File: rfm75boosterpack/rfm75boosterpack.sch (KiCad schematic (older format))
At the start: 4 parts, among them J1 Ti_Booster_J1, U1 RFM75

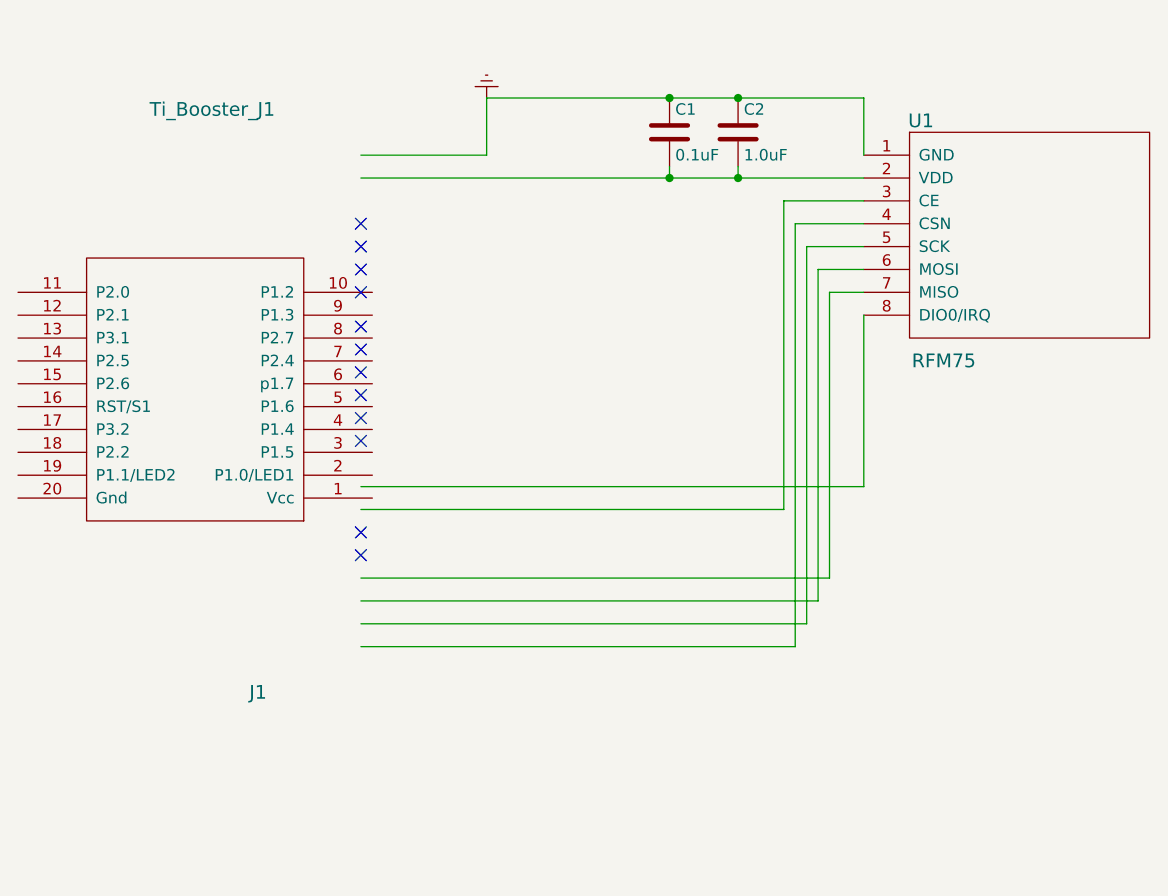
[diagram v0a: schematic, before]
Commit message: Correct boosterpack component, replace, and reroute. Also regen gerbers.
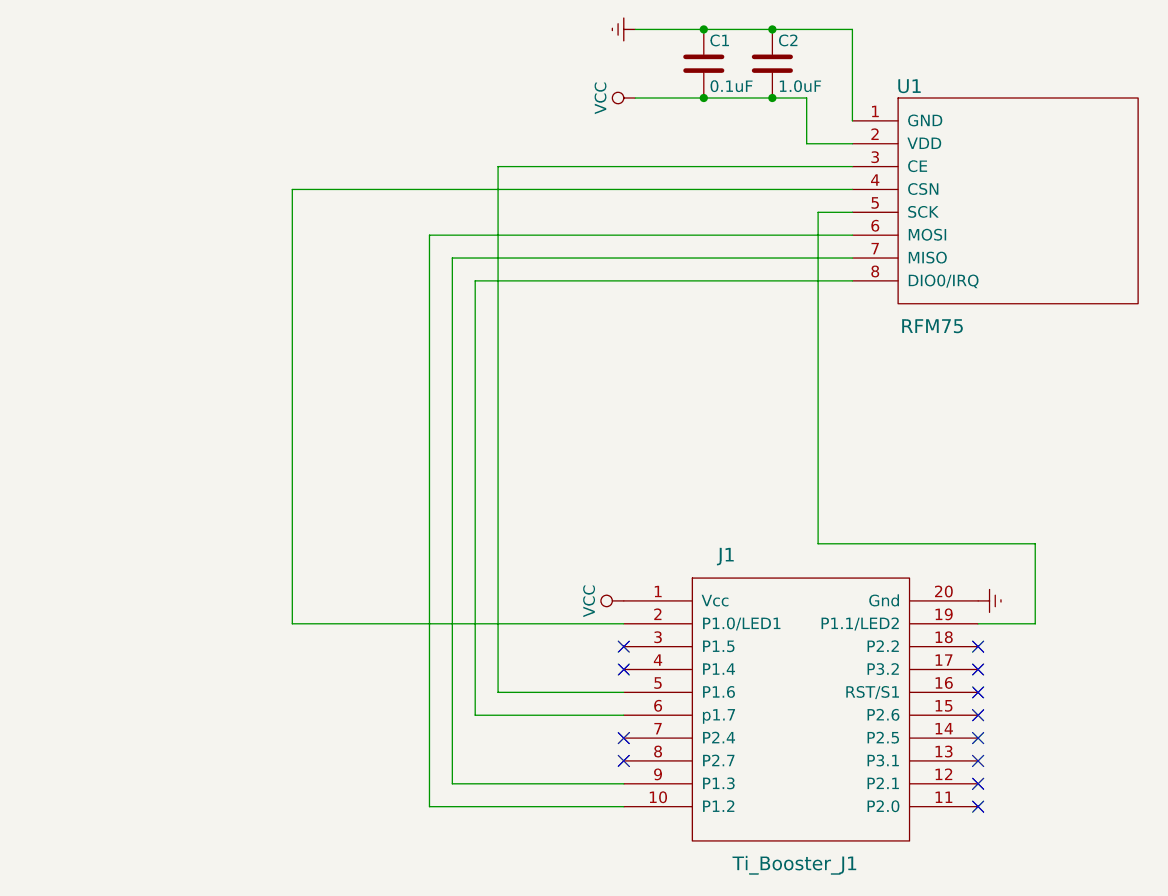
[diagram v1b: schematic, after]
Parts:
- J1: footprint boosterpack20:BoosterPack_J1_J2 -> (none)
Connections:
- net labels added: VCC
- wire segments 24 -> 25
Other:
- moved on the sheet: C1, C2, U1
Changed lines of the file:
@@
 EESchema Schematic File Version 2
+LIBS:rfm75boosterpack-rescue
 LIBS:power
 LIBS:device
@@
 LIBS:boosterpack
 LIBS:rfm75
+LIBS:rfm75boosterpack-cache
 EELAYER 25 0
 EELAYER END
@@
 $EndDescr
 $Comp
-L Ti_Booster_J1 J1
-U 1 1 5B2155AA
-P 3200 3100
-F 0 "J1" H 2900 4400 60  0000 C CNN
-F 1 "Ti_Booster_J1" H 3100 1850 60  0000 C CNN
-F 2 "boosterpack20:BoosterPack_J1_J2" H 3200 3100 60  0001 C CNN
-F 3 "" H 3200 3100 60  0000 C CNN
-	1    3200 3100
-	-1   0    0    1
-$EndComp
-$Comp
 L RFM75 U1
 U 1 1 5B2156FD
-P 6300 2750
-F 0 "U1" H 6400 3600 60  0000 C CNN
-F 1 "RFM75" H 6500 2550 60  0000 C CNN
-F 2 "rfm75:RFM75" H 6300 2750 60  0001 C CNN
-F 3 "" H 6300 2750 60  0001 C CNN
-	1    6300 2750
-	1    0    0    -1
-$EndComp
-$Comp
-L Earth #PWR01
-U 1 1 5B2158AA
-P 4500 1800
-F 0 "#PWR01" H 4500 1550 50  0001 C CNN
-F 1 "Earth" H 4500 1650 50  0001 C CNN
-F 2 "" H 4500 1800 50  0001 C CNN
-F 3 "" H 4500 1800 50  0001 C CNN
-	1    4500 1800
-	-1   0    0    1
+P 6250 2600
+F 0 "U1" H 6350 3450 60  0000 C CNN
+F 1 "RFM75" H 6450 2400 60  0000 C CNN
+F 2 "rfm75:RFM75" H 6250 2600 60  0001 C CNN
+F 3 "" H 6250 2600 60  0001 C CNN
+	1    6250 2600
+	1    0    0    -1
 $EndComp
 $Comp
 L C C2
 U 1 1 5B2158C6
-P 5600 1950
-F 0 "C2" H 5625 2050 50  0000 L CNN
-F 1 "1.0uF" H 5625 1850 50  0000 L CNN
-F 2 "Capacitors_SMD:C_0805_HandSoldering" H 5638 1800 50  0001 C CNN
-F 3 "" H 5600 1950 50  0001 C CNN
-	1    5600 1950
+P 5750 1650
+F 0 "C2" H 5775 1750 50  0000 L CNN
+F 1 "1.0uF" H 5775 1550 50  0000 L CNN
+F 2 "Capacitors_SMD:C_0805_HandSoldering" H 5788 1500 50  0001 C CNN
+F 3 "" H 5750 1650 50  0001 C CNN
+	1    5750 1650
 	1    0    0    -1
 $EndComp
@@
 L C C1
 U 1 1 5B21590A
-P 5300 1950
-F 0 "C1" H 5325 2050 50  0000 L CNN
-F 1 "0.1uF" H 5325 1850 50  0000 L CNN
-F 2 "Capacitors_SMD:C_0805_HandSoldering" H 5338 1800 50  0001 C CNN
-F 3 "" H 5300 1950 50  0001 C CNN
-	1    5300 1950
-	1    0    0    -1
-$EndComp
-Wire Wire Line
-	3950 4200 5850 4200
-Wire Wire Line
-	5900 4100 3950 4100
-Wire Wire Line
-	5950 4000 3950 4000
-Wire Wire Line
-	3950 3900 6000 3900
-Wire Wire Line
-	5850 4200 5850 2350
-Wire Wire Line
-	5900 2450 5900 4100
-Wire Wire Line
-	6000 3900 6000 2650
-Wire Wire Line
-	5950 2550 5950 4000
-Wire Wire Line
-	6150 3500 6150 2750
-Wire Wire Line
-	5800 3600 5800 2250
-Wire Wire Line
-	3950 3600 5800 3600
-Wire Wire Line
-	5800 2250 6150 2250
-Wire Wire Line
-	5850 2350 6150 2350
-Wire Wire Line
-	5900 2450 6150 2450
-Wire Wire Line
-	6150 2550 5950 2550
-Wire Wire Line
-	6000 2650 6150 2650
-Wire Wire Line
-	3950 3500 6150 3500
-Wire Wire Line
-	3950 2150 6150 2150
-Wire Wire Line
-	6150 1800 6150 2050
-Wire Wire Line
-	4500 1800 6150 1800
-Connection ~ 5300 2150
-Wire Wire Line
-	5300 2150 5300 2100
-Wire Wire Line
-	5600 2150 5600 2100
-Connection ~ 5600 2150
-Connection ~ 5600 1800
-Connection ~ 5300 1800
-Wire Wire Line
-	4500 2050 4500 1800
-Wire Wire Line
-	3950 2050 4500 2050
-NoConn ~ 3950 3800
-NoConn ~ 3950 3700
-NoConn ~ 3950 3300
-NoConn ~ 3950 3200
-NoConn ~ 3950 3100
-NoConn ~ 3950 3000
-NoConn ~ 3950 2900
-NoConn ~ 3950 2800
-NoConn ~ 3950 2650
-NoConn ~ 3950 2550
-NoConn ~ 3950 2450
-NoConn ~ 3950 2350
+P 5450 1650
+F 0 "C1" H 5475 1750 50  0000 L CNN
+F 1 "0.1uF" H 5475 1550 50  0000 L CNN
+F 2 "Capacitors_SMD:C_0805_HandSoldering" H 5488 1500 50  0001 C CNN
+F 3 "" H 5450 1650 50  0001 C CNN
+	1    5450 1650
+	1    0    0    -1
+$EndComp
+$Comp
+L Ti_Booster_J1 J1
+U 1 1 5B28B197
+P 5900 4450
+F 0 "J1" H 5550 5100 60  0000 C CNN
+F 1 "Ti_Booster_J1" H 5850 3750 60  0000 C CNN
+F 2 "" H 5900 3900 60  0000 C CNN
+F 3 "" H 5900 3900 60  0000 C CNN
+	1    5900 4450
+	1    0    0    -1
+$EndComp
+$Comp
+L Earth #PWR01
+U 1 1 5B28B3AA
+P 6650 4000
+F 0 "#PWR01" H 6650 3750 50  0001 C CNN
+F 1 "Earth" H 6650 3850 50  0001 C CNN
+F 2 "" H 6650 4000 50  0001 C CNN
+F 3 "" H 6650 4000 50  0001 C CNN
+	1    6650 4000
+	0    -1   -1   0
+$EndComp
+$Comp
+L VCC #PWR02
+U 1 1 5B28B3C6
+P 5100 4000
+F 0 "#PWR02" H 5100 3850 50  0001 C CNN
+F 1 "VCC" H 5100 4150 50  0000 C CNN
+F 2 "" H 5100 4000 50  0001 C CNN
+F 3 "" H 5100 4000 50  0001 C CNN
+	1    5100 4000
+	0    -1   -1   0
+$EndComp
+Wire Wire Line
+	3650 2200 6100 2200
+Wire Wire Line
+	3650 4100 5100 4100
+Wire Wire Line
+	6650 4100 6900 4100
+Wire Wire Line
+	6900 4100 6900 3750
+Wire Wire Line
+	6900 3750 5950 3750
+Wire Wire Line
+	5950 3750 5950 2300
+Wire Wire Line
+	5950 2300 6100 2300
+Wire Wire Line
+	3650 4100 3650 2200
+Wire Wire Line
+	5100 4800 4350 4800
+Wire Wire Line
+	4350 4800 4350 2500
+Wire Wire Line
+	4350 2500 6100 2500
+Wire Wire Line
+	5100 4900 4250 4900
+Wire Wire Line
+	4250 4900 4250 2400
+Wire Wire Line
+	4250 2400 6100 2400
+Wire Wire Line
+	6100 2600 4450 2600
+Wire Wire Line
+	4450 2600 4450 4500
+Wire Wire Line
+	4450 4500 5100 4500
+Wire Wire Line
+	6100 2100 4550 2100
+Wire Wire Line
+	4550 2100 4550 4400
+Wire Wire Line
+	4550 4400 5100 4400
+Wire Wire Line
+	6100 1500 6100 1900
+Connection ~ 5750 1500
+Connection ~ 5450 1500
+$Comp
+L Earth #PWR03
+U 1 1 5B28B738
+P 5150 1500
+F 0 "#PWR03" H 5150 1250 50  0001 C CNN
+F 1 "Earth" H 5150 1350 50  0001 C CNN
+F 2 "" H 5150 1500 50  0001 C CNN
+F 3 "" H 5150 1500 50  0001 C CNN
+	1    5150 1500
+	0    1    1    0
+$EndComp
+$Comp
+L VCC #PWR04
+U 1 1 5B28B80F
+P 5150 1800
+F 0 "#PWR04" H 5150 1650 50  0001 C CNN
+F 1 "VCC" H 5150 1950 50  0000 C CNN
+F 2 "" H 5150 1800 50  0001 C CNN
+F 3 "" H 5150 1800 50  0001 C CNN
+	1    5150 1800
+	0    -1   -1   0
+$EndComp
+Wire Wire Line
+	5150 1500 6100 1500
+Wire Wire Line
+	6100 2000 5900 2000
+Wire Wire Line
+	5900 2000 5900 1800
+Wire Wire Line
+	5900 1800 5150 1800
+Connection ~ 5750 1800
+Connection ~ 5450 1800
+NoConn ~ 5100 4200
+NoConn ~ 5100 4300
+NoConn ~ 5100 4600
+NoConn ~ 5100 4700
+NoConn ~ 6650 4900
+NoConn ~ 6650 4800
+NoConn ~ 6650 4700
+NoConn ~ 6650 4600
+NoConn ~ 6650 4500
+NoConn ~ 6650 4400
+NoConn ~ 6650 4300
+NoConn ~ 6650 4200
 $EndSCHEMATC
